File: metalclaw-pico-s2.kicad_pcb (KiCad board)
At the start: 2 copper layers, 21 x 51 mm, 54 parts, among them J1 USB_C_Receptacle_USB2.0_14P, J2 Conn_01x05, J3 Conn_02x05_Odd_Even, U1 ESP32-S2, U2 MX25L3236FM2I-08G-TR, U3 APS6404L-3SQRx-SN, U5 XC6220B331MR, Y1 XRCGB40M000F1S2FR0

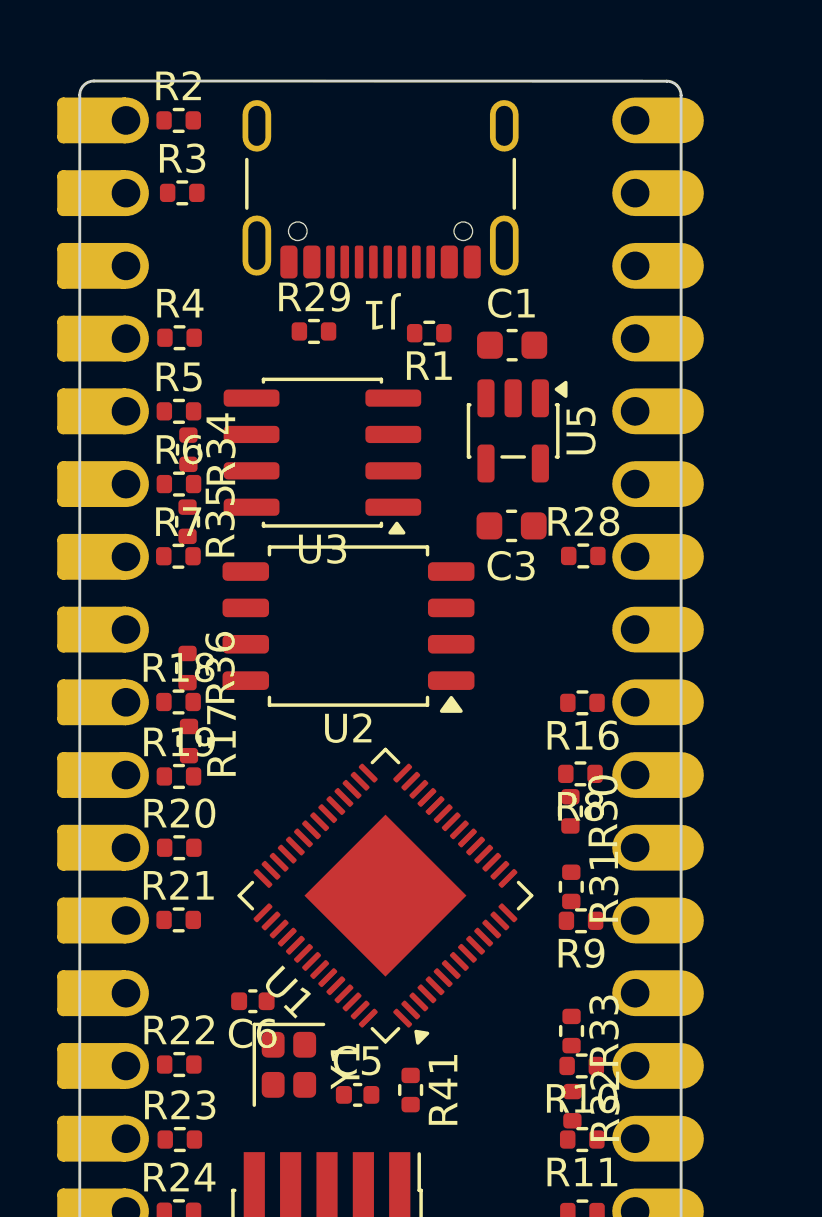
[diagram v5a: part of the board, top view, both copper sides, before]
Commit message: Add keepouts for Pi Pico pins
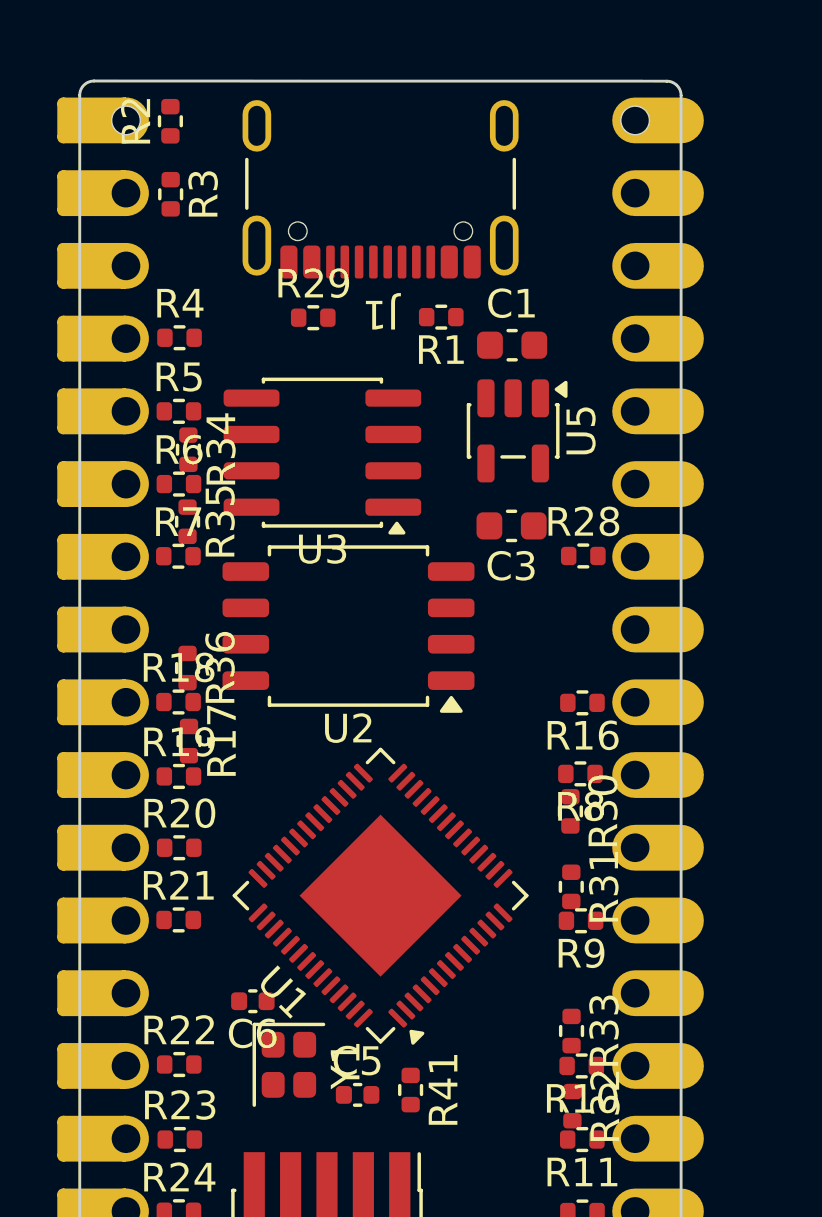
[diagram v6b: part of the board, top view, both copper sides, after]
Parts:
- moved R1 0.70 mm to (165.9, 81.6)
- moved R29 0.48 mm to (161.5, 81.6)
- moved R3 0.41 mm to (156.5, 77.3), turned to -90 degrees
- moved R2 0.29 mm to (156.5, 74.8), turned to 90 degrees
- moved U1 0.17 mm to (163.8, 101.8)
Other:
- outline, holes or cut-outs redrawn
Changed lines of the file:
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@@
 	(footprint "Resistor_SMD:R_0402_1005Metric"
 		(layer "F.Cu")
-		(at 161.485 82.11)
+		(at 161.46 81.63)
 		(descr "Resistor SMD 0402 (1005 Metric), square (rectangular) end terminal, IPC-7351 nominal, (Body size source: IPC-SM-782 page 72, https://www.pcb-3d.com/wordpress/wp-content/uploads/ipc-sm-782a_amendment_1_and_2.pdf), generated with kicad-footprint-generator")
 		(tags "resistor")
@@
 	(footprint "Resistor_SMD:R_0402_1005Metric"
 		(layer "F.Cu")
-		(at 156.885 77.27)
+		(at 156.48 77.32 -90)
 		(descr "Resistor SMD 0402 (1005 Metric), square (rectangular) end terminal, IPC-7351 nominal, (Body size source: IPC-SM-782 page 72, https://www.pcb-3d.com/wordpress/wp-content/uploads/ipc-sm-782a_amendment_1_and_2.pdf), generated with kicad-footprint-generator")
 		(tags "resistor")
 		(property "Reference" "R3"
-			(at 0 -1.17 0)
+			(at 0 -1.17 90)
 			(layer "F.SilkS")
 			(effects
@@
 		)
 		(property "Value" "220"
-			(at 0 1.17 0)
+			(at 0 1.17 90)
 			(layer "F.Fab")
 			(effects
@@
 		)
 		(property "Datasheet" "~"
-			(at 0 0 0)
+			(at 0 0 90)
 			(layer "F.Fab")
 			(hide yes)
@@
 		)
 		(property "Description" "Resistor, US symbol"
-			(at 0 0 0)
+			(at 0 0 90)
 			(layer "F.Fab")
 			(hide yes)
@@
 		)
 		(property "KLC_S3.3" ""
-			(at 0 0 0)
+			(at 0 0 270)
 			(unlocked yes)
 			(layer "F.Fab")
@@
 		)
 		(property "KLC_S4.1" ""
-			(at 0 0 0)
+			(at 0 0 270)
 			(unlocked yes)
 			(layer "F.Fab")
@@
 		(attr smd)
 		(fp_line
-			(start -0.153641 -0.38)
-			(end 0.153641 -0.38)
+			(start -0.153641 0.38)
+			(end 0.153641 0.38)
 			(stroke
 				(width 0.12)
@@
 		)
 		(fp_line
-			(start -0.153641 0.38)
-			(end 0.153641 0.38)
+			(start -0.153641 -0.38)
+			(end 0.153641 -0.38)
 			(stroke
 				(width 0.12)
@@
 		)
 		(fp_text user "${REFERENCE}"
-			(at 0 0 0)
+			(at 0 0 90)
 			(layer "F.Fab")
 			(effects
@@
 		)
 		(pad "1" smd roundrect
-			(at -0.51 0)
+			(at -0.51 0 270)
 			(size 0.54 0.64)
 			(layers "F.Cu" "F.Mask" "F.Paste")
@@
 		)
 		(pad "2" smd roundrect
-			(at 0.51 0)
+			(at 0.51 0 270)
 			(size 0.54 0.64)
 			(layers "F.Cu" "F.Mask" "F.Paste")
@@
 	(footprint "Resistor_SMD:R_0402_1005Metric"
 		(layer "F.Cu")
-		(at 165.51 82.17 180)
+		(at 165.93 81.61 180)
 		(descr "Resistor SMD 0402 (1005 Metric), square (rectangular) end terminal, IPC-7351 nominal, (Body size source: IPC-SM-782 page 72, https://www.pcb-3d.com/wordpress/wp-content/uploads/ipc-sm-782a_amendment_1_and_2.pdf), generated with kicad-footprint-generator")
 		(tags "resistor")
@@
 	(footprint "Resistor_SMD:R_0402_1005Metric"
 		(layer "F.Cu")
-		(at 156.76 74.74)
+		(at 156.47 74.77 90)
 		(descr "Resistor SMD 0402 (1005 Metric), square (rectangular) end terminal, IPC-7351 nominal, (Body size source: IPC-SM-782 page 72, https://www.pcb-3d.com/wordpress/wp-content/uploads/ipc-sm-782a_amendment_1_and_2.pdf), generated with kicad-footprint-generator")
 		(tags "resistor")
 		(property "Reference" "R2"
-			(at 0 -1.17 0)
+			(at 0 -1.17 90)
 			(layer "F.SilkS")
 			(effects
@@
 		)
 		(property "Value" "220"
-			(at 0 1.17 0)
+			(at 0 1.17 90)
 			(layer "F.Fab")
 			(effects
@@
 		)
 		(property "Datasheet" "~"
-			(at 0 0 0)
+			(at 0 0 90)
 			(layer "F.Fab")
 			(hide yes)
@@
 		)
 		(property "Description" "Resistor, US symbol"
-			(at 0 0 0)
+			(at 0 0 90)
 			(layer "F.Fab")
 			(hide yes)
@@
 		)
 		(property "KLC_S3.3" ""
-			(at 0 0 0)
+			(at 0 0 90)
 			(unlocked yes)
 			(layer "F.Fab")
@@
 		)
 		(property "KLC_S4.1" ""
-			(at 0 0 0)
+			(at 0 0 90)
 			(unlocked yes)
 			(layer "F.Fab")
@@
 		)
 		(fp_text user "${REFERENCE}"
-			(at 0 0 0)
+			(at 0 0 90)
 			(layer "F.Fab")
 			(effects
@@
 		)
 		(pad "1" smd roundrect
-			(at -0.51 0)
+			(at -0.51 0 90)
 			(size 0.54 0.64)
 			(layers "F.Cu" "F.Mask" "F.Paste")
@@
 		)
 		(pad "2" smd roundrect
-			(at 0.51 0)
+			(at 0.51 0 90)
 			(size 0.54 0.64)
 			(layers "F.Cu" "F.Mask" "F.Paste")
@@
 			(layer "Edge.Cuts")
 		)
+		(fp_circle
+			(center -8.89 -24.13)
+			(end -8.39 -24.13)
+			(stroke
+				(width 0.05)
+				(type solid)
+			)
+			(fill no)
+			(layer "Edge.Cuts")
+		)
+		(fp_circle
+			(center 8.89 -24.13)
+			(end 9.39 -24.13)
+			(stroke
+				(width 0.05)
+				(type solid)
+			)
+			(fill no)
+			(layer "Edge.Cuts")
+		)
+		(fp_rect
+			(start -10.66 -25.91)
+			(end -7.12 25.9)
+			(stroke
+				(width 0.05)
+				(type solid)
+			)
+			(fill no)
+			(layer "F.CrtYd")
+		)
+		(fp_rect
+			(start 7.12 -25.91)
+			(end 10.66 25.9)
+			(stroke
+				(width 0.05)
+				(type solid)
+			)
+			(fill no)
+			(layer "F.CrtYd")
+		)
+		(fp_line
+			(start -10.16 -24.765)
+			(end -9.525 -25.4)
+			(stroke
+				(width 0.1)
+				(type solid)
+			)
+			(layer "F.Fab")
+		)
+		(fp_line
+			(start -10.16 25.4)
+			(end -10.16 -24.765)
+			(stroke
+				(width 0.1)
+				(type solid)
+			)
+			(layer "F.Fab")
+		)
+		(fp_line
+			(start -9.525 -25.4)
+			(end -7.62 -25.4)
+			(stroke
+				(width 0.1)
+				(type solid)
+			)
+			(layer "F.Fab")
+		)
+		(fp_line
+			(start -7.62 -25.4)
+			(end -7.62 25.4)
+			(stroke
+				(width 0.1)
+				(type solid)
+			)
+			(layer "F.Fab")
+		)
+		(fp_line
+			(start -7.62 25.4)
+			(end -10.16 25.4)
+			(stroke
+				(width 0.1)
+				(type solid)
+			)
+			(layer "F.Fab")
+		)
+		(fp_line
+			(start 7.62 -24.765)
+			(end 8.255 -25.4)
+			(stroke
+				(width 0.1)
+				(type solid)
+			)
+			(layer "F.Fab")
+		)
+		(fp_line
+			(start 7.62 25.4)
+			(end 7.62 -24.765)
+			(stroke
+				(width 0.1)
+				(type solid)
+			)
+			(layer "F.Fab")
+		)
+		(fp_line
+			(start 8.255 -25.4)
+			(end 10.16 -25.4)
+			(stroke
+				(width 0.1)
+				(type solid)
+			)
+			(layer "F.Fab")
+		)
+		(fp_line
+			(start 10.16 -25.4)
+			(end 10.16 25.4)
+			(stroke
+				(width 0.1)
+				(type solid)
+			)
+			(layer "F.Fab")
+		)
+		(fp_line
+			(start 10.16 25.4)
+			(end 7.62 25.4)
+			(stroke
+				(width 0.1)
+				(type solid)
+			)
+			(layer "F.Fab")
+		)
 		(fp_text user "Keep Out"
 			(at -0.004831 -36.195 0)
@@
 			(pintype "bidirectional")
 		)
+		(group ""
+			(members "0088f66f-2c1c-4549-b57d-51e849f3a661" "1e28adc4-6e32-4c8d-91fb-4efe23107fdb"
+				"25c03a40-3758-4e9c-86a4-b8e8b1e1d281" "58e852b3-c587-4edd-9417-5b5ea51549f8"
+				"596b30e1-653f-4477-a8d0-e39a29e6e4d1" "78dd4d97-157a-40de-b21e-ffacef240d14"
+				"90375648-f577-4a62-80f8-9c6463c678ca"
+			)
+		)
+		(group ""
+			(members "19a1e68d-5110-417e-ab2e-85d80fb00297" "5edabd42-5618-4b38-9575-d4dbfd4b9a4d"
+				"ab1bc576-1067-4059-96d3-fd00402276dd" "c2a3cfbc-75e5-4667-aead-bb0be52f7546"
+				"dde067f5-85c0-4c24-9980-781f232c44ed" "e34747ce-c455-48e7-abad-72cc9dd2f35f"
+				"f462b17d-6e28-4748-a6d4-532ac3a8eb50"
+			)
+		)
 		(embedded_fonts no)
 	)
@@
 	)
 	(footprint "Package_DFN_QFN:QFN-56-1EP_7x7mm_P0.4mm_EP4x4mm"
+		(locked yes)
 		(layer "F.Cu")
-		(at 163.981041 101.812004 135)
+		(at 163.81 101.812004 135)
 		(descr "QFN, 56 Pin (https://www.espressif.com/sites/default/files/documentation/esp32-s2_datasheet_en.pdf#page=41), generated with kicad-footprint-generator ipc_noLead_generator.py")
 		(tags "QFN NoLead")

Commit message: Refine schematic and layout more
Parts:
- added C12: C, Capacitor_SMD:C_0402_1005Metric, F.Cu at (165.4, 107.7)
- added C13: C, Capacitor_SMD:C_0402_1005Metric, F.Cu at (169.0, 108.3)
- added J4: Conn_Coaxial, Connector_Coaxial:U.FL_Hirose_U.FL-R-SMT-1_Vertical, F.Cu at (168.4, 111.2)
- added L1: L, Inductor_SMD:L_0402_1005Metric, F.Cu at (167.4, 106.6)
- added R42: 5.1k, Resistor_SMD:R_0402_1005Metric, F.Cu at (180.0, 82.6)
- added SW1: SW_Push, Button_Switch_SMD:SW_Push_SPST_NO_Alps_SKRK, F.Cu at (159.5, 82.5)
- added SW2: SW_Push, Button_Switch_SMD:SW_Push_SPST_NO_Alps_SKRK, F.Cu at (168.1, 82.5)
- moved R29 9.24 mm to (170.1, 78.3), turned to -90 degrees
- moved R28 8.45 mm to (167.3, 97.6)
- moved R33 7.99 mm to (168.1, 114.2), turned to 0 degrees
- moved R1 7.44 mm to (170.1, 75.5), turned to -90 degrees
- moved R32 6.74 mm to (168.6, 115.6), turned to 90 degrees
- moved R4 6.56 mm to (158.7, 88.6)
- moved R10 6.47 mm to (170.0, 114.2)
- moved R5 5.79 mm to (161.1, 88.8)
- moved R38 5.49 mm to (168.6, 117.5), turned to -90 degrees
- moved R36 5.21 mm to (157.7, 99.0), turned to 180 degrees
- moved R11 4.89 mm to (170.0, 115.1)
- moved R16 4.81 mm to (166.2, 96.5)
- moved R34 3.88 mm to (158.9, 89.7), turned to 0 degrees
- moved R35 3.84 mm to (157.2, 92.6), turned to 90 degrees
- moved U5 3.35 mm to (167.5, 88.8), turned to 0 degrees
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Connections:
- C1 pad 1: VBUS -> VS
- J2 pad 5: Net-(J2-Pin_5) -> /RESET
- R41 pad 2: Net-(J2-Pin_5) -> /3V3_EN
- U1 pad 2: unconnected-(U1-LNA_IN-Pad2) -> Net-(U1-LNA_IN)
- U1 pad 56: Net-(J2-Pin_5) -> /RESET
- U5 pad 1: VBUS -> VS
- U5 pad 3: VBUS -> VS

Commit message: Assign more part numbers
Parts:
- added C10: 1u, Capacitor_SMD:C_0402_1005Metric, F.Cu at (181.3, 101.8)
- added C11: 1u, Capacitor_SMD:C_0402_1005Metric, F.Cu at (184.2, 92.0)
- added C14: 100n, Capacitor_SMD:C_0201_0603Metric, F.Cu at (184.2, 93.9)
- added C15: 100n, Capacitor_SMD:C_0201_0603Metric, F.Cu at (184.2, 95.9)
- added C16: 100n, Capacitor_SMD:C_0201_0603Metric, F.Cu at (184.2, 97.9)
- added C17: 100n, Capacitor_SMD:C_0201_0603Metric, F.Cu at (184.2, 99.8)
- added C2: 1u, Capacitor_SMD:C_0402_1005Metric, F.Cu at (181.3, 92.0)
- added C4: 100n, Capacitor_SMD:C_0201_0603Metric, F.Cu at (181.3, 93.9)
- added C7: 100n, Capacitor_SMD:C_0201_0603Metric, F.Cu at (181.3, 95.9)
- added C8: 100n, Capacitor_SMD:C_0201_0603Metric, F.Cu at (181.3, 97.9)
- added C9: 100n, Capacitor_SMD:C_0201_0603Metric, F.Cu at (181.3, 99.8)
- added D1: D_Schottky, Diode_SMD:D_SOD-323F, F.Cu at (170.0, 76.3)
- C12, C13, C5, C6: footprint Capacitor_SMD:C_0402_1005Metric -> Capacitor_SMD:C_0201_0603Metric
- L1: footprint Inductor_SMD:L_0402_1005Metric -> Inductor_SMD:L_0201_0603Metric
- R1, R10, R11, R12, R13, R14, R15, R16, R17, R18, R19, R2, R20, R21, R22, R23, R24, R25, R26, R27, R28, R29, R3, R30, R31, R32, R33, R34, R35, R36, R37, R38, R39, R4, R40, R41, R42, R5, R6, R7, R8, R9: footprint Resistor_SMD:R_0402_1005Metric -> Resistor_SMD:R_0201_0603Metric
- SW1, SW2: footprint Button_Switch_SMD:SW_Push_SPST_NO_Alps_SKRK -> Button_Switch_SMD:SW_SPST_PTS810
- moved SW1 0.10 mm to (159.5, 82.6)
- moved SW2 0.09 mm to (168.1, 82.6)
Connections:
- R17 pad 2: /GP7 -> /GP6
- R19 pad 2: /GP7 -> /GP6
- R27 pad 2: /GP15 -> /GP14
- R31 pad 2: /GP15 -> /GP14
- R40 pad 2: /GP15 -> /GP14
- U1 pad 21: /GP7 -> /GP6
- U1 pad 55: /GP15 -> /GP14
